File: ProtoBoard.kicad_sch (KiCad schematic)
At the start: 52 parts, among them IC1 L9110S, IC2 L9110S, IC3 L9110S, J1 Conn_01x02_Female, J11 Conn_01x10_Female, J2 Conn_01x08_Female, J3 I2C_STANDARDQWIIC, J4 Conn_01x10_Female, J5 Conn_01x05_Female, J6 Conn_01x05_Female, J7 Conn_01x10_Female, J8 Conn_01x05_Female, J9 Conn_01x10_Female, U1 ESP32-WROOM-32D, U10 SY6280AAC, U2 CD74HC4067SM, U3 LM1084-5.0, U4 CD74HC4067SM, U6 LM1084-3.3, U7 SY6280AAC, U8 SY6280AAC, U9 SY6280AAC

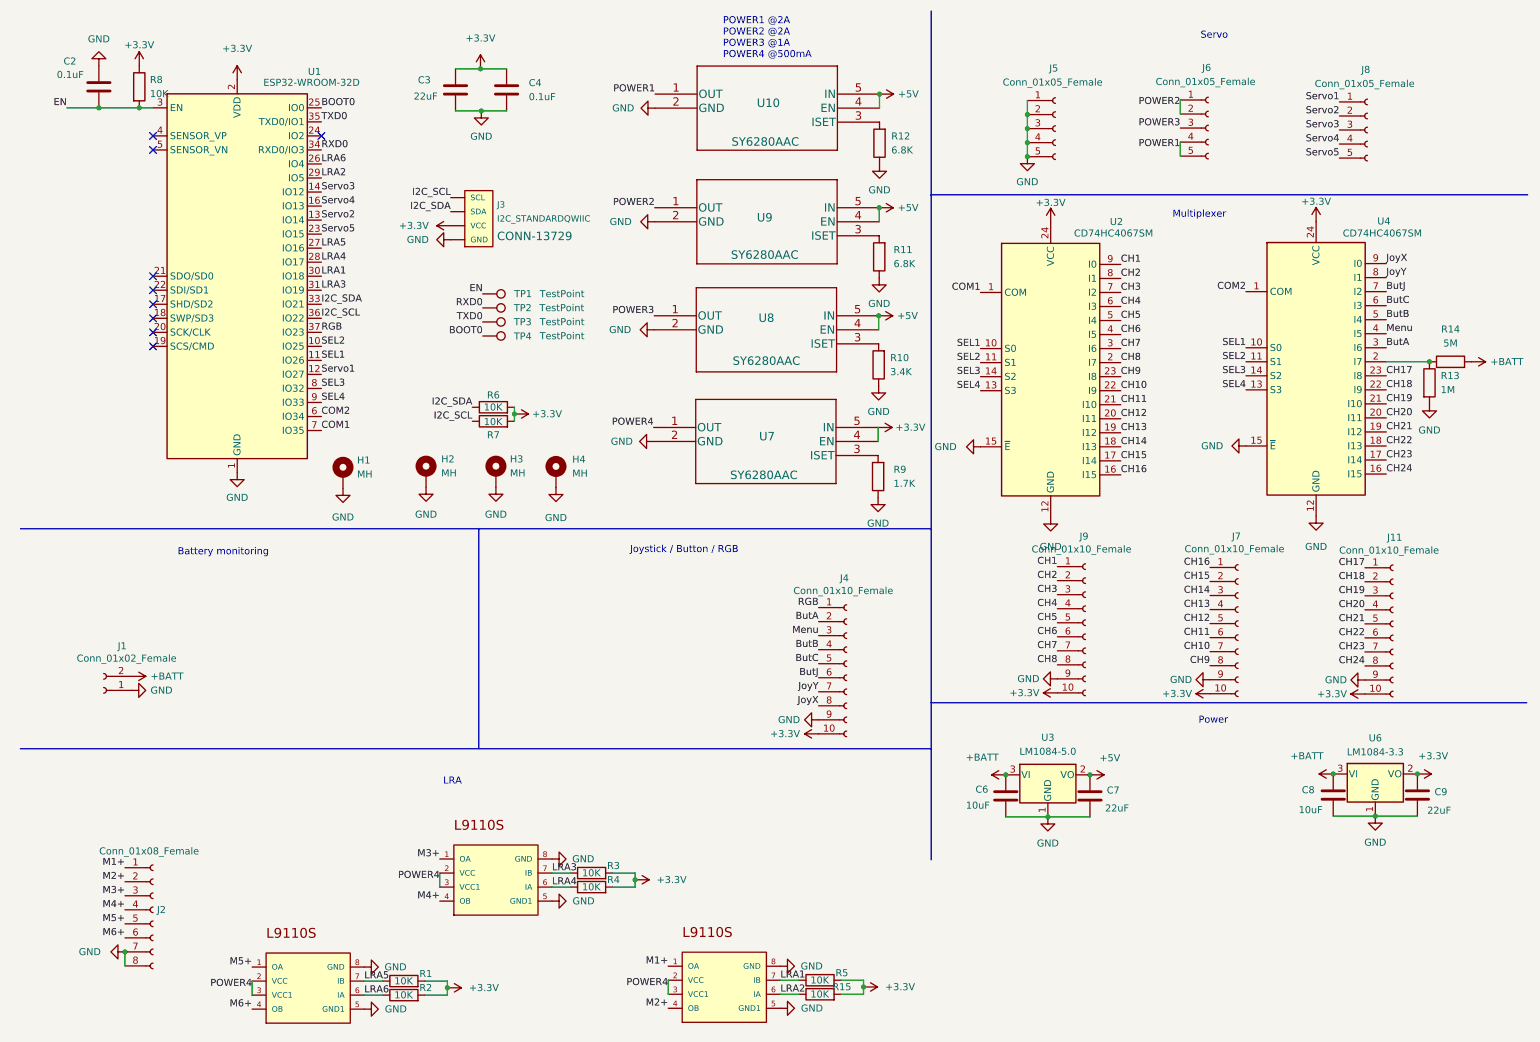
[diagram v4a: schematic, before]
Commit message: Add bms + switch to esp32s3 + USB C + 8 LRA driver
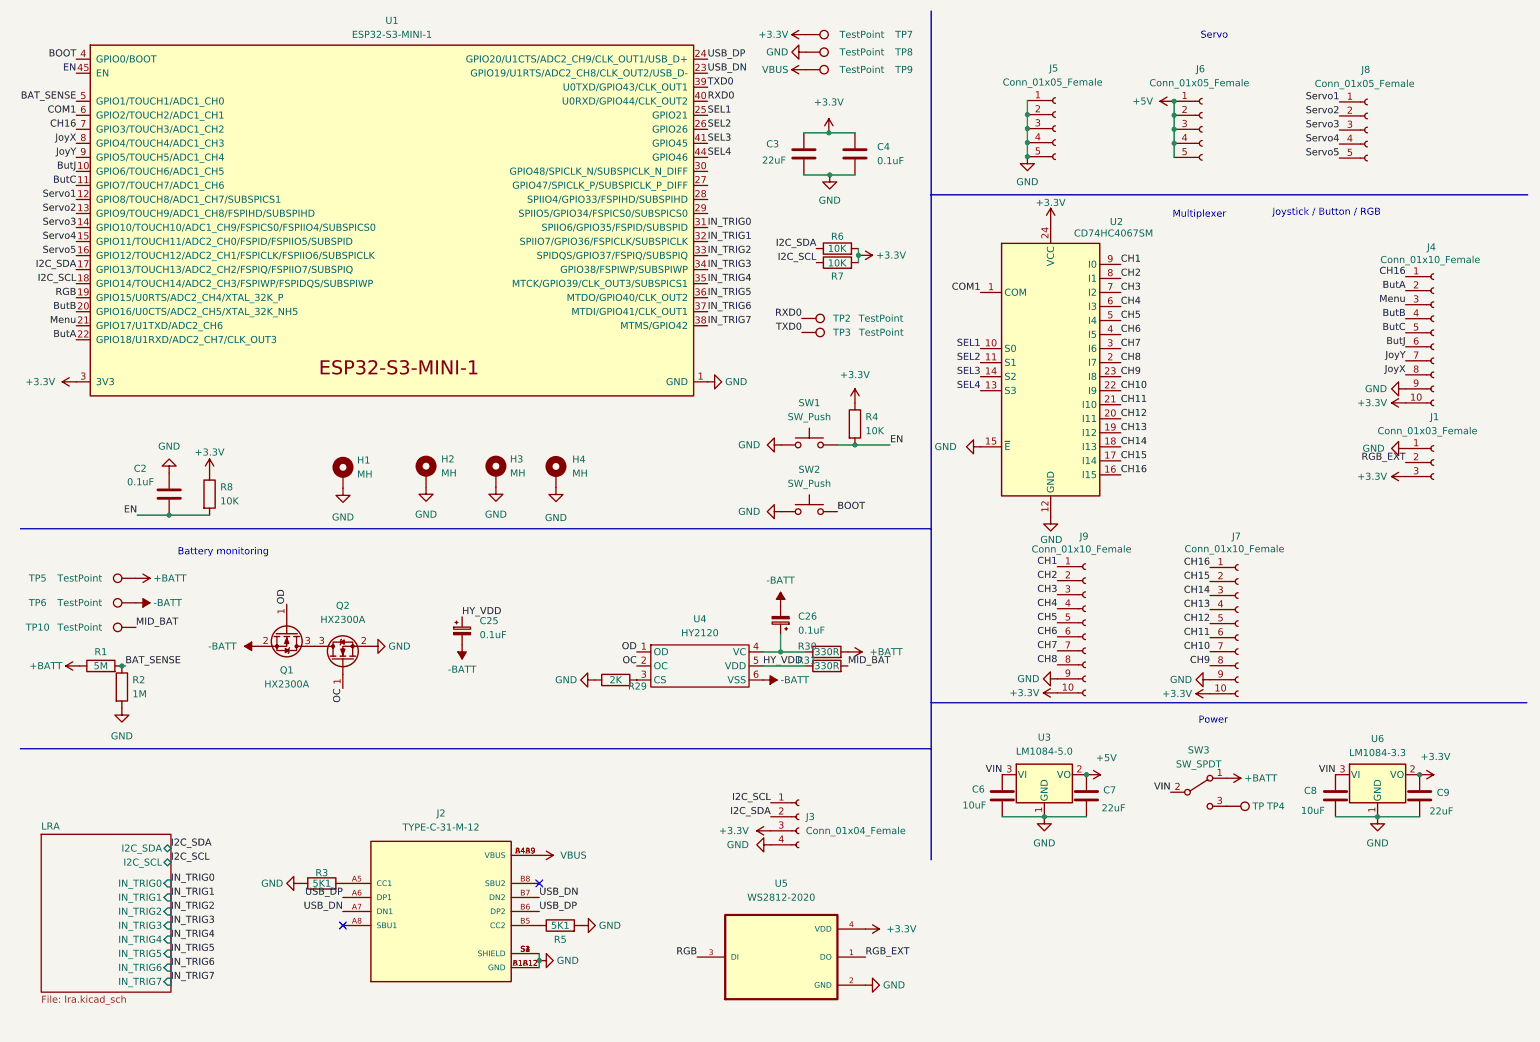
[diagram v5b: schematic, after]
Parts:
- removed IC1, IC2, IC3: L9110S, footprints:SOIC127P600X150-8, symbol L9110S:L9110S
- removed J1: Conn_01x02_Female, Connector_PinHeader_2.54mm:PinHeader_1x02_P2.54mm_Vertical, symbol Connector:Conn_01x02_Female
- removed J11: Conn_01x10_Female, Connector_JST:JST_GH_SM10B-GHS-TB_1x10-1MP_P1.25mm_Horizontal, symbol Connector:Conn_01x10_Female
- removed J2: Conn_01x08_Female, Connector_JST:JST_GH_SM08B-GHS-TB_1x08-1MP_P1.25mm_Horizontal, symbol Connector:Conn_01x08_Female
- removed J3: I2C_STANDARDQWIIC, Connectors:1X04_1MM_RA, symbol SparkFun-Connectors:I2C_STANDARDQWIIC
- removed R10: 3.4K, Resistor_SMD:R_0402_1005Metric, symbol Device:R
- removed R11, R12: 6.8K, Resistor_SMD:R_0402_1005Metric, symbol Device:R
- removed R13: 1M, Resistor_SMD:R_0402_1005Metric, symbol Device:R
- removed R14: 5M, Resistor_SMD:R_0402_1005Metric, symbol Device:R
- removed R15: 10K, Resistor_SMD:R_0402_1005Metric, symbol Device:R
- removed R9: 1.7K, Resistor_SMD:R_0402_1005Metric, symbol Device:R
- removed TP1: TestPoint, TestPoint:TestPoint_Pad_D1.5mm, symbol Connector:TestPoint
- removed U1: ESP32-WROOM-32D, RF_Module:ESP32-WROOM-32, symbol RF_Module:ESP32-WROOM-32D
- removed U10, U7, U8, U9: SY6280AAC, footprints:SY6280AAC, symbol 2022-04-08_21-45-33:SY6280AAC
- removed U4: CD74HC4067SM, Package_SO:SSOP-24_5.3x8.2mm_P0.65mm, symbol 74xx:CD74HC4067SM
- added C25, C26: 0.1uF, Capacitor_SMD:CP_Elec_4x5.4, symbol Device:C_Polarized_Small
- added J1: Conn_01x03_Female, Connector_PinHeader_2.54mm:PinHeader_1x03_P2.54mm_Vertical, symbol Connector:Conn_01x03_Female
- added J2: TYPE-C-31-M-12, TYPE-C-31-M-12:HRO_TYPE-C-31-M-12, symbol TYPE-C-31-M-12:TYPE-C-31-M-12
- added J3: Conn_01x04_Female, Connector_PinHeader_2.54mm:PinHeader_1x04_P2.54mm_Vertical, symbol Connector:Conn_01x04_Female
- added Q1, Q2: HX2300A, Package_TO_SOT_SMD:SOT-23, symbol Transistor_FET:2N7002E
- added R29: 2K, Resistor_SMD:R_0402_1005Metric, symbol Device:R
- added R30, R31: 330R, Resistor_SMD:R_0402_1005Metric, symbol Device:R
- added SW1, SW2: SW_Push, Button_Switch_SMD:SW_Push_SPST_NO_Alps_SKRK, symbol Switch:SW_Push
- added SW3: SW_SPDT, Button_Switch_SMD:SW_SPDT_PCM12, symbol Switch:SW_SPDT
- added TP10, TP5, TP6, TP7, TP8, TP9: TestPoint, TestPoint:TestPoint_Pad_D1.5mm, symbol Connector:TestPoint
- added U1: ESP32-S3-MINI-1, Espressif:ESP32-S3-MINI-1, symbol Espressif:ESP32-S3-MINI-1
- added U4: HY2120, Package_TO_SOT_SMD:SOT-23-6, symbol dextra:HY2120
- added U5: WS2812-2020, WS2812-2020:LED_WS2812-2020, symbol WS2812-2020:WS2812-2020
- J4, J7, J9: footprint Connector_JST:JST_GH_SM10B-GHS-TB_1x10-1MP_P1.25mm_Horizontal -> Connector_PinHeader_2.54mm:PinHeader_1x10_P2.54mm_Vertical
- R1: value 10K -> 5M
- R2: value 10K -> 1M
- R3, R5: value 10K -> 5K1
- TP4: value TestPoint -> TP
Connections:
- net LRA3 is gone; now on net GND: R3.1
- net LRA4 is gone; now on net +3V3: R4.1
- net LRA5 is gone; now on net +BATT: R1.1
- net POWER1 is gone; now on net +5V: J6.4 (Pin_4), J6.5 (Pin_5)
- net POWER2 is gone; now on net +5V: J6.1 (Pin_1), J6.2 (Pin_2)
- net POWER3 is gone; now on net +5V: J6.3 (Pin_3)
- net +3V3: now also J1.3 (Pin_3), J3.3 (Pin_3), TP7.1, U1.3 (3V3), U5.4 (VDD); no longer R1.2, R2.2, R3.2, R4.2, R5.2
- net +BATT: now also R30.2, SW3.1 (A), TP5.1; no longer C6.1, C8.1, U3.3 (VI), U6.3 (VI)
- net ButA: now also U1.22 (GPIO18/U1RXD/ADC2_CH7/CLK_OUT3)
- net ButB: now also U1.20 (GPIO16/U0CTS/ADC2_CH5/XTAL_32K_NH5)
- net ButC: now also U1.11 (GPIO7/TOUCH7/ADC1_CH6)
- net ButJ: now also U1.10 (GPIO6/TOUCH6/ADC1_CH5)
- net CH16: now also J4.1 (Pin_1), U1.7 (GPIO3/TOUCH3/ADC1_CH2)
- net COM1: now also U1.6 (GPIO2/TOUCH2/ADC1_CH1)
- net EN: now also R4.2, SW1.2, U1.45 (EN)
- net GND: now also R2.2, R5.2, J1.1 (Pin_1), J2.A1B12 (GND), J2.B1A12 (GND), J2.S1 (SHIELD), J2.S2 (SHIELD), J2.S3 (SHIELD), J2.S4 (SHIELD), J3.4 (Pin_4), Q2.2 (S), R29.1, SW1.1, SW2.1, TP8.1, U1.1 (GND), U1.2 (GND), U1.42 (GND), U1.43 (GND), U1.46 (GND), U1.47 (GND), U1.48 (GND), U1.49 (GND), U1.50 (GND), U1.51 (GND), U1.52 (GND), U1.53 (GND), U1.54 (GND), U1.55 (GND), U1.56 (GND), U1.57 (GND), U1.58 (GND), U1.59 (GND), U1.60 (GND), U1.61 (GND), U1.62 (GND), U1.63 (GND), U1.64 (GND), U1.65 (GND), U5.2 (GND)
- net I2C_SCL: now also J3.1 (Pin_1), U1.18 (GPIO14/TOUCH14/ADC2_CH3/FSPIWP/FSPIDQS/SUBSPIWP)
- net I2C_SDA: now also J3.2 (Pin_2), U1.17 (GPIO13/TOUCH13/ADC2_CH2/FSPIQ/FSPIIO7/SUBSPIQ)
- net JoyX: now also U1.8 (GPIO4/TOUCH4/ADC1_CH3)
- net JoyY: now also U1.9 (GPIO5/TOUCH5/ADC1_CH4)
- net Menu: now also U1.21 (GPIO17/U1TXD/ADC2_CH6)
- net RGB: now also U1.19 (GPIO15/U0RTS/ADC2_CH4/XTAL_32K_P), U5.3 (DI); no longer J4.1 (Pin_1)
- net RXD0: now also U1.40 (U0RXD/GPIO44/CLK_OUT2)
- net SEL1: now also U1.25 (GPIO21)
- net SEL2: now also U1.26 (GPIO26)
- net SEL3: now also U1.41 (GPIO45)
- net SEL4: now also U1.44 (GPIO46)
- net Servo1: now also U1.12 (GPIO8/TOUCH8/ADC1_CH7/SUBSPICS1)
- net Servo2: now also U1.13 (GPIO9/TOUCH9/ADC1_CH8/FSPIHD/SUBSPIHD)
- net Servo3: now also U1.14 (GPIO10/TOUCH10/ADC1_CH9/FSPICS0/FSPIIO4/SUBSPICS0)
- net Servo4: now also U1.15 (GPIO11/TOUCH11/ADC2_CH0/FSPID/FSPIIO5/SUBSPID)
- net Servo5: now also U1.16 (GPIO12/TOUCH12/ADC2_CH1/FSPICLK/FSPIIO6/SUBSPICLK)
- net TXD0: now also U1.39 (U0TXD/GPIO43/CLK_OUT1)
- net BOOT0: no longer names the net of TP4.1
- net BOOT0: now also SW3.3 (C)
- net LRA1: no longer names the net of R5.1
- net LRA1: now also J2.B5 (CC2)
- net LRA6 renamed BAT_SENSE
- net BAT_SENSE: now also R1.2, U1.5 (GPIO1/TOUCH1/ADC1_CH0)
- new net: Q1.3 (D), Q2.3 (D)
- new net: C26.1, R30.1, U4.4 (VC)
- new net: R29.2, U4.3 (CS)
- new net: J2.A5 (CC1), R3.2
- new net -BATT: C25.2, C26.2, Q1.2 (S), TP6.1, U4.6 (VSS)
- new net BOOT: SW2.2, U1.4 (GPIO0/BOOT)
- new net HY_VDD: C25.1, R31.1, U4.5 (VDD)
- new net IN_TRIG0: U1.31 (SPIIO6/GPIO35/FSPID/SUBSPID)
- new net IN_TRIG1: U1.32 (SPIIO7/GPIO36/FSPICLK/SUBSPICLK)
- new net IN_TRIG2: U1.33 (SPIDQS/GPIO37/FSPIQ/SUBSPIQ)
- new net IN_TRIG3: U1.34 (GPIO38/FSPIWP/SUBSPIWP)
- new net IN_TRIG4: U1.35 (MTCK/GPIO39/CLK_OUT3/SUBSPICS1)
- new net IN_TRIG5: U1.36 (MTDO/GPIO40/CLK_OUT2)
- new net IN_TRIG6: U1.37 (MTDI/GPIO41/CLK_OUT1)
- new net IN_TRIG7: U1.38 (MTMS/GPIO42)
- new net MID_BAT: R31.2, TP10.1
- new net OC: Q2.1 (G), U4.2 (OC)
- new net OD: Q1.1 (G), U4.1 (OD)
- new net RGB_EXT: J1.2 (Pin_2), U5.1 (DO)
- new net USB_DN: J2.A7 (DN1), J2.B7 (DN2), U1.23 (GPIO19/U1RTS/ADC2_CH8/CLK_OUT2/USB_D-)
- new net USB_DP: J2.A6 (DP1), J2.B6 (DP2), U1.24 (GPIO20/U1CTS/ADC2_CH9/CLK_OUT1/USB_D+)
- new net VBUS: J2.A4B9 (VBUS), J2.B4A9 (VBUS), TP9.1
- new net VIN: C6.1, C8.1, SW3.2 (B), U3.3 (VI), U6.3 (VI)
- no-connect marks 9 -> 2
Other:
- added sheet LRA (lra.kicad_sch)
- note removed: "LRA"
- note removed: "POWER1 @2A POWER2 @2A POWER3 @1A POWER4 @500mA"
- moved on the sheet: C2, C3, C4, C6, C7, J4, J6, R6, R7, R8, TP2, TP3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

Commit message: Routing WIP
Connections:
- net ButA: now also U1.19 (GPIO15/U0RTS/ADC2_CH4/XTAL_32K_P); no longer U1.22 (GPIO18/U1RXD/ADC2_CH7/CLK_OUT3)
- net ButB: now also U1.17 (GPIO13/TOUCH13/ADC2_CH2/FSPIQ/FSPIIO7/SUBSPIQ); no longer U1.20 (GPIO16/U0CTS/ADC2_CH5/XTAL_32K_NH5)
- net ButC: now also U1.15 (GPIO11/TOUCH11/ADC2_CH0/FSPID/FSPIIO5/SUBSPID); no longer U1.11 (GPIO7/TOUCH7/ADC1_CH6)
- net ButJ: now also U1.14 (GPIO10/TOUCH10/ADC1_CH9/FSPICS0/FSPIIO4/SUBSPICS0); no longer U1.10 (GPIO6/TOUCH6/ADC1_CH5)
- net CH1: now also J9.4 (Pin_4); no longer J9.1 (Pin_1)
- net CH10: now also J9.5 (Pin_5); no longer J7.7 (Pin_7)
- net CH12: now also J9.6 (Pin_6); no longer J7.5 (Pin_5)
- net CH13: now also J7.7 (Pin_7); no longer J7.4 (Pin_4)
- net CH14: now also J9.7 (Pin_7); no longer J7.3 (Pin_3)
- net CH15: now also J7.8 (Pin_8); no longer J7.2 (Pin_2)
- net CH16: now also J9.8 (Pin_8); no longer J4.1 (Pin_1), J7.1 (Pin_1), U1.7 (GPIO3/TOUCH3/ADC1_CH2)
- net CH2: now also J7.4 (Pin_4); no longer J9.2 (Pin_2)
- net CH4: now also J7.3 (Pin_3); no longer J9.4 (Pin_4)
- net CH5: now also J9.2 (Pin_2); no longer J9.5 (Pin_5)
- net CH6: now also J7.2 (Pin_2); no longer J9.6 (Pin_6)
- net CH7: now also J7.1 (Pin_1); no longer J9.7 (Pin_7)
- net CH8: now also J9.1 (Pin_1); no longer J9.8 (Pin_8)
- net CH9: now also J7.5 (Pin_5); no longer J7.8 (Pin_8)
- net I2C_SCL: now also U1.21 (GPIO17/U1TXD/ADC2_CH6); no longer U1.18 (GPIO14/TOUCH14/ADC2_CH3/FSPIWP/FSPIDQS/SUBSPIWP)
- net I2C_SDA: now also U1.22 (GPIO18/U1RXD/ADC2_CH7/CLK_OUT3); no longer U1.17 (GPIO13/TOUCH13/ADC2_CH2/FSPIQ/FSPIIO7/SUBSPIQ)
- net IN_TRIG0: now also U1.35 (MTCK/GPIO39/CLK_OUT3/SUBSPICS1); no longer U1.31 (SPIIO6/GPIO35/FSPID/SUBSPID)
- net IN_TRIG1: now also U1.36 (MTDO/GPIO40/CLK_OUT2); no longer U1.32 (SPIIO7/GPIO36/FSPICLK/SUBSPICLK)
- net IN_TRIG2: now also U1.37 (MTDI/GPIO41/CLK_OUT1); no longer U1.33 (SPIDQS/GPIO37/FSPIQ/SUBSPIQ)
- net IN_TRIG3: now also U1.38 (MTMS/GPIO42); no longer U1.34 (GPIO38/FSPIWP/SUBSPIWP)
- net IN_TRIG4: now also U1.11 (GPIO7/TOUCH7/ADC1_CH6); no longer U1.35 (MTCK/GPIO39/CLK_OUT3/SUBSPICS1)
- net IN_TRIG5: now also U1.10 (GPIO6/TOUCH6/ADC1_CH5); no longer U1.36 (MTDO/GPIO40/CLK_OUT2)
- net IN_TRIG6: now also U1.9 (GPIO5/TOUCH5/ADC1_CH4); no longer U1.37 (MTDI/GPIO41/CLK_OUT1)
- net IN_TRIG7: now also U1.8 (GPIO4/TOUCH4/ADC1_CH3); no longer U1.38 (MTMS/GPIO42)
- net JoyX: now also U1.12 (GPIO8/TOUCH8/ADC1_CH7/SUBSPICS1); no longer U1.8 (GPIO4/TOUCH4/ADC1_CH3)
- net JoyY: now also U1.13 (GPIO9/TOUCH9/ADC1_CH8/FSPIHD/SUBSPIHD); no longer U1.9 (GPIO5/TOUCH5/ADC1_CH4)
- net Menu: now also U1.18 (GPIO14/TOUCH14/ADC2_CH3/FSPIWP/FSPIDQS/SUBSPIWP); no longer U1.21 (GPIO17/U1TXD/ADC2_CH6)
- net RGB: now also U1.7 (GPIO3/TOUCH3/ADC1_CH2); no longer U1.19 (GPIO15/U0RTS/ADC2_CH4/XTAL_32K_P)
- net SEL1: now also U1.28 (SPIIO4/GPIO33/FSPIHD/SUBSPIHD); no longer U1.25 (GPIO21)
- net SEL2: now also U1.27 (GPIO47/SPICLK_P/SUBSPICLK_P_DIFF); no longer U1.26 (GPIO26)
- net SEL3: now also U1.25 (GPIO21); no longer U1.41 (GPIO45)
- net SEL4: now also U1.26 (GPIO26); no longer U1.44 (GPIO46)
- net Servo1: now also U1.34 (GPIO38/FSPIWP/SUBSPIWP); no longer U1.12 (GPIO8/TOUCH8/ADC1_CH7/SUBSPICS1)
- net Servo2: now also U1.33 (SPIDQS/GPIO37/FSPIQ/SUBSPIQ); no longer U1.13 (GPIO9/TOUCH9/ADC1_CH8/FSPIHD/SUBSPIHD)
- net Servo3: now also U1.32 (SPIIO7/GPIO36/FSPICLK/SUBSPICLK); no longer U1.14 (GPIO10/TOUCH10/ADC1_CH9/FSPICS0/FSPIIO4/SUBSPICS0)
- net Servo4: now also U1.31 (SPIIO6/GPIO35/FSPID/SUBSPID); no longer U1.15 (GPIO11/TOUCH11/ADC2_CH0/FSPID/FSPIIO5/SUBSPID)
- net Servo5: now also U1.30 (GPIO48/SPICLK_N/SUBSPICLK_N_DIFF); no longer U1.16 (GPIO12/TOUCH12/ADC2_CH1/FSPICLK/FSPIIO6/SUBSPICLK)
- new net GPIO: J4.1 (Pin_1), U1.20 (GPIO16/U0CTS/ADC2_CH5/XTAL_32K_NH5)
- no-connect marks 2 -> 4

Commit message: Routing done, silkscreen cleaning, update README, remove old files
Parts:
- removed SW3: SW_SPDT, Button_Switch_SMD:SW_SPDT_PCM12, symbol Switch:SW_SPDT
- removed TP4: TP, TestPoint:TestPoint_Pad_D1.5mm, symbol Connector:TestPoint
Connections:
- net VIN is gone; now on net +BATT: C6.1, C8.1, U3.3 (VI), U6.3 (VI)
- net I2C_SCL: now also J3.2 (Pin_2); no longer J3.1 (Pin_1)
- net I2C_SDA: now also J3.1 (Pin_1); no longer J3.2 (Pin_2)
- net IN_TRIG7: no longer U1.8 (GPIO4/TOUCH4/ADC1_CH3)
- no-connect marks 4 -> 7
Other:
- moved on the sheet: C6, C7, C8, C9, U3, U6
